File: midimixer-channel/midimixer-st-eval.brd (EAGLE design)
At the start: 50.8 x 71.1 mm, 63 parts, among them IC3 74LS595D, IC4 74165D, U1 LM1117IMPX-3.3/NOPB, Y1 8MHz 695-HCM49-8-U

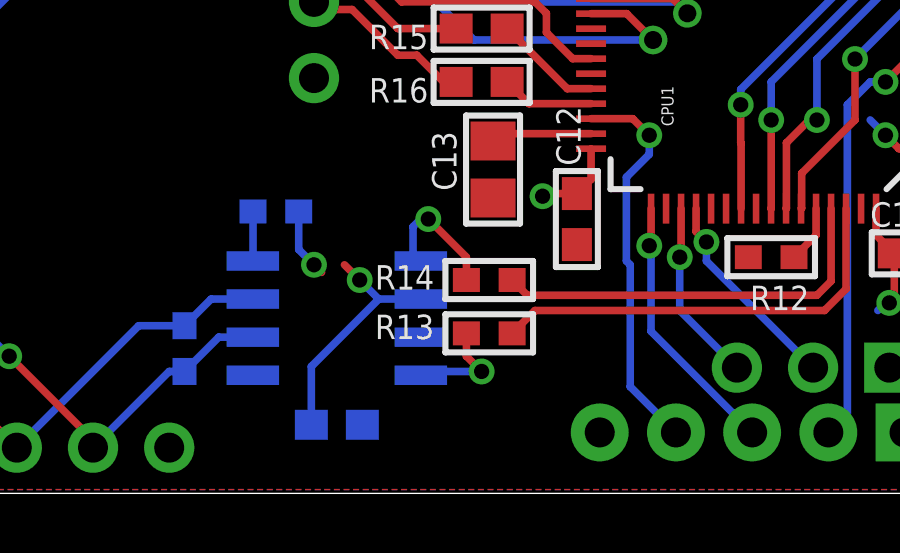
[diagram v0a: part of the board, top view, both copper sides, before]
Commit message: fix can tx<->rx (flip them)
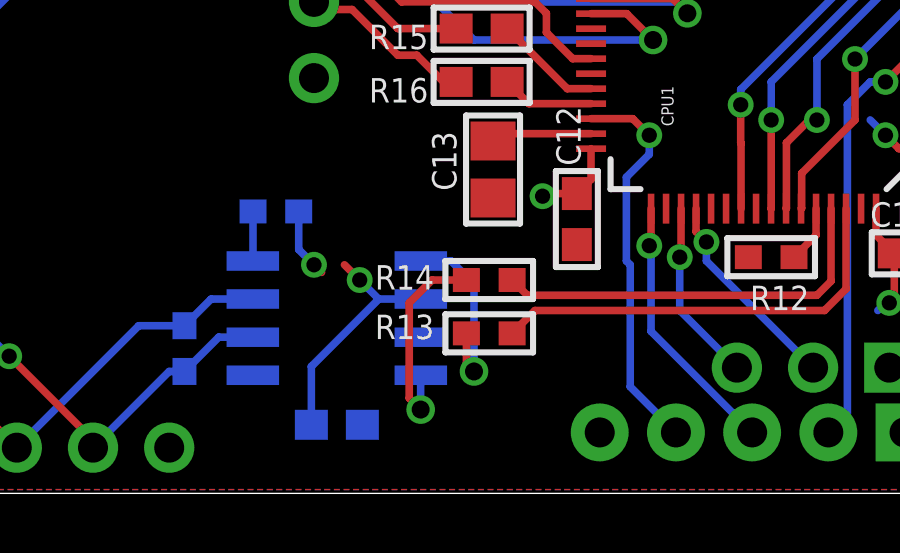
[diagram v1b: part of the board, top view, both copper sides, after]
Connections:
- net CAN_RX: now also R14.1; no longer R13.1
- net CAN_TX: now also R13.1; no longer R14.1
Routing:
- net CAN_RX: track 3.56 -> 7.26 mm
- net CAN_TX: track 4.42 -> 6.38 mm
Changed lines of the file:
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@@
 <?xml version="1.0" encoding="utf-8"?>
 <!DOCTYPE eagle SYSTEM "eagle.dtd">
-<eagle version="7.6.0">
+<eagle version="7.2.0">
 <drawing>
 <settings>
@@
 </signal>
 <signal name="CAN_TX">
-<contactref element="R14" pad="1"/>
-<wire x1="24.384" y1="7.112" x2="24.384" y2="7.874" width="0.254" layer="1"/>
-<wire x1="24.384" y1="7.874" x2="23.114" y2="9.144" width="0.254" layer="1"/>
-<via x="23.114" y="9.144" extent="1-16" drill="0.508"/>
-<wire x1="23.114" y1="9.144" x2="22.86" y2="9.144" width="0.254" layer="16"/>
-<wire x1="22.86" y1="9.144" x2="22.606" y2="8.89" width="0.254" layer="16"/>
-<wire x1="22.606" y1="8.89" x2="22.606" y2="8.007" width="0.254" layer="16"/>
 <contactref element="D2" pad="1"/>
-<wire x1="22.866" y1="7.747" x2="22.606" y2="8.007" width="0.254" layer="16"/>
+<contactref element="R13" pad="1"/>
+<wire x1="24.384" y1="5.334" x2="24.384" y2="4.318" width="0.254" layer="1"/>
+<via x="24.638" y="4.064" extent="1-16" drill="0.6"/>
+<wire x1="24.638" y1="4.064" x2="24.638" y2="6.985" width="0.254" layer="16"/>
+<wire x1="24.638" y1="6.985" x2="23.876" y2="7.747" width="0.254" layer="16"/>
+<wire x1="23.876" y1="7.747" x2="22.866" y2="7.747" width="0.254" layer="16"/>
+<wire x1="24.384" y1="4.318" x2="24.638" y2="4.064" width="0.254" layer="1"/>
 </signal>
 <signal name="CAN_RX">
 <contactref element="D2" pad="4"/>
-<contactref element="R13" pad="1"/>
-<wire x1="24.384" y1="5.334" x2="24.384" y2="4.572" width="0.254" layer="1"/>
-<wire x1="24.384" y1="4.572" x2="24.892" y2="4.064" width="0.254" layer="1"/>
-<via x="24.892" y="4.064" extent="1-16" drill="0.508"/>
-<wire x1="24.892" y1="4.064" x2="22.993" y2="4.064" width="0.254" layer="16"/>
 <wire x1="22.993" y1="4.064" x2="22.866" y2="3.937" width="0.254" layer="16"/>
+<contactref element="R14" pad="1"/>
+<wire x1="24.384" y1="7.112" x2="23.241" y2="7.112" width="0.254" layer="1"/>
+<wire x1="23.241" y1="7.112" x2="22.479" y2="6.35" width="0.254" layer="1"/>
+<wire x1="22.479" y1="6.35" x2="22.479" y2="3.175" width="0.254" layer="1"/>
+<wire x1="22.479" y1="3.175" x2="22.86" y2="2.794" width="0.254" layer="1"/>
+<via x="22.86" y="2.794" extent="1-16" drill="0.6"/>
+<wire x1="22.86" y1="2.794" x2="22.86" y2="3.931" width="0.254" layer="16"/>
+<wire x1="22.86" y1="3.931" x2="22.866" y2="3.937" width="0.254" layer="16"/>
 </signal>
 <signal name="SPI2_RC2">
